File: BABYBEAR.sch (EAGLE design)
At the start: 63 parts, among them IC1 ATMEGA1284P, IC2 ATMEGA16U2-MU, IC3 MC33269DT-5.0, IC4 LM358D, IC5 LP2985-33DBVR, J1 Power, J2 Analog, J3 Digital_8_13, J4 Digital_0_7, J5 DC_2_1MM, P1 USB-6PSMT, P2 ICSP:MAIN, P3 ICSP:USB, P5V M01SMD, Q1 FDN340P, Q2 2N7002, X1 16MHz, X2 16MHz

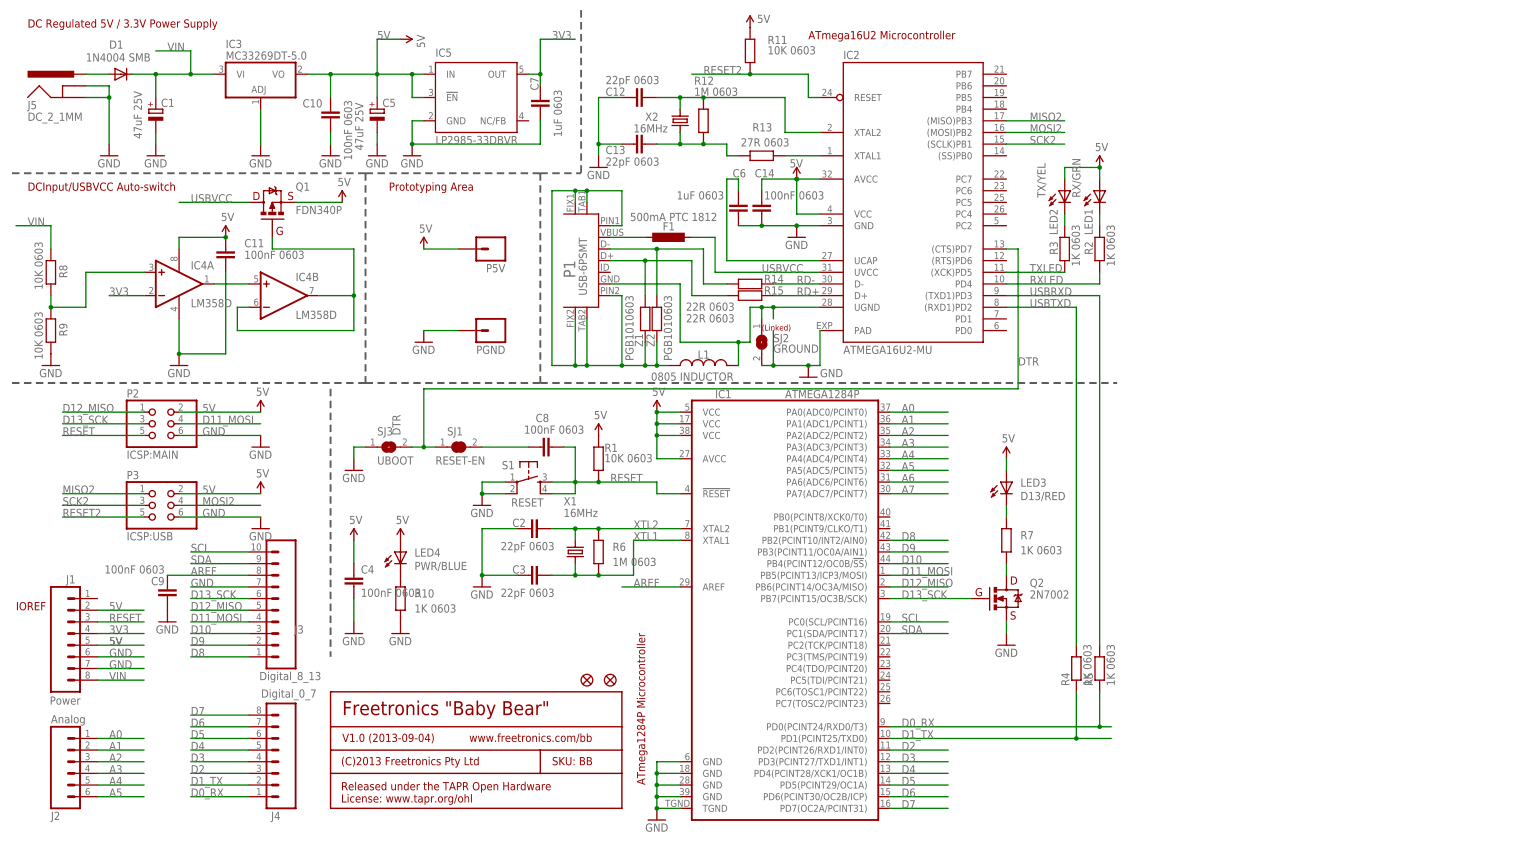
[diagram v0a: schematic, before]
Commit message: Changed USB connector to USB-C for v2.0 release
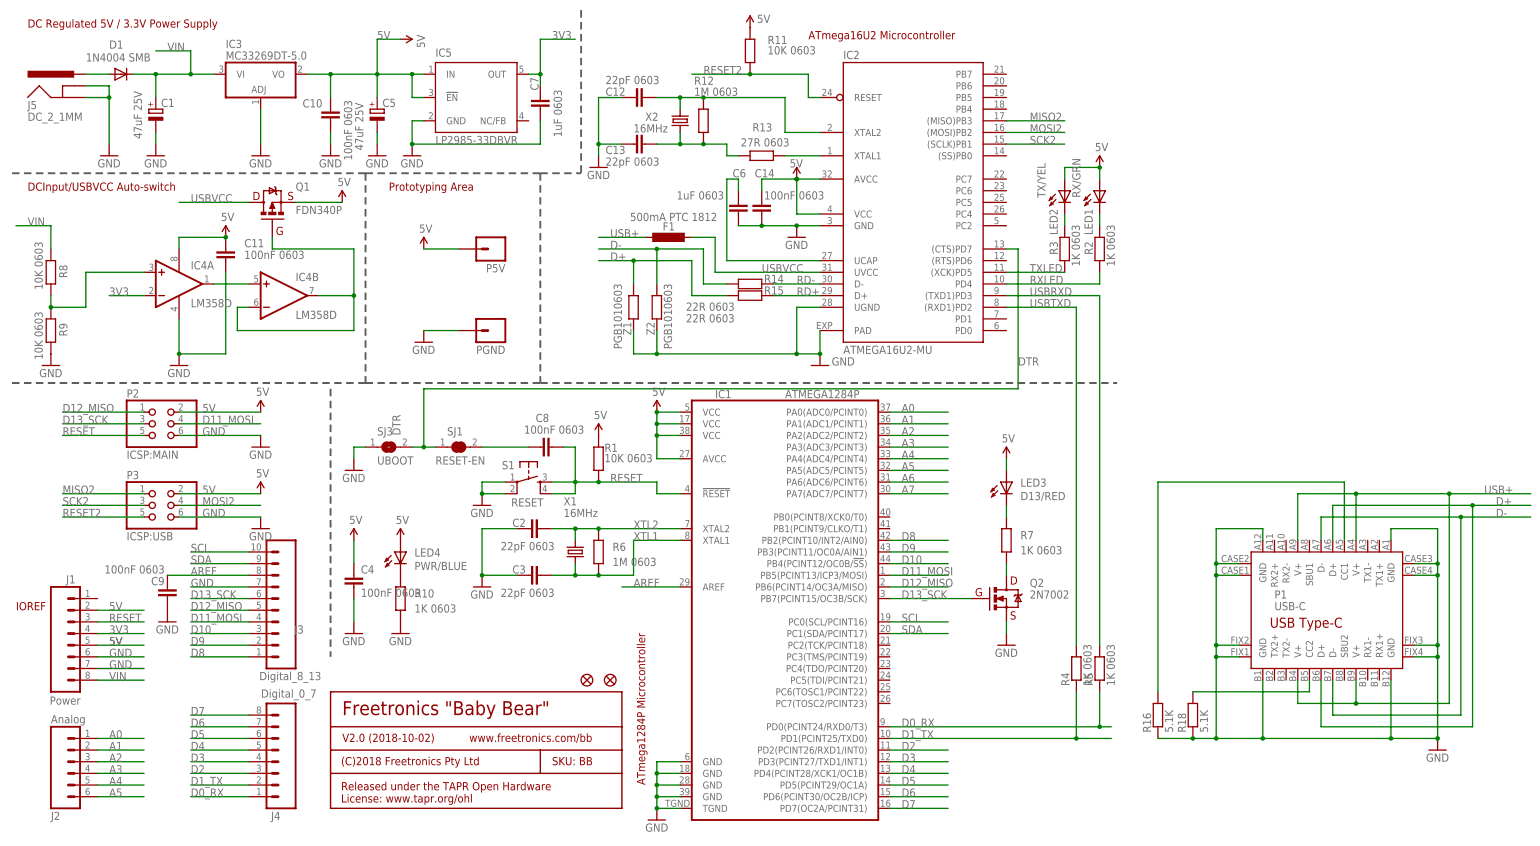
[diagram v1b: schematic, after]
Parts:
- removed L1: 0805 INDUCTOR, freetronics-master-v1:INDUCTOR0805-LARGE
- removed SJ2: GROUND, jumper:SJ
- added R16, R18: 5.1K, freetronics-original:RESISTOR0603
- J5: device freetronics:POWER_JACKPTH -> freetronics-jon:POWER_JACKPTH_SLOTS
- P1: value USB-6PSMT -> USB-C; device freetronics-jon:USB-6PSMT -> freetronics-jon:USB-C
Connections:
- removed net N$115: F1.1, P1.VBUS
- removed net N$16: P1.D+, R15.2, Z1.1
- removed net N$17: P1.D-, R14.2, Z2.1
- removed net UGND: IC2.UGND, L1.2, P1.GND, SJ2.1
- new net D+: P1.D+@A6, P1.D+@B6, R15.2, Z1.1
- new net D-: P1.D-@A7, P1.D-@B7, R14.2, Z2.1
- new net N$7: P1.CC1, R16.2
- new net USB+: F1.1, P1.V+@A4, P1.V+@A9, P1.V+@B4, P1.V+@B9
- net GND: now also IC2.UGND, P1.GND@A1, P1.GND@A12, P1.GND@B1, P1.GND@B12, P1.GND@CASE1, P1.GND@CASE2, P1.GND@CASE3, P1.GND@CASE4, P1.GND@FIX1, P1.GND@FIX2, P1.GND@FIX3, P1.GND@FIX4, R16.1, R18.1, Z1.2, Z2.2; no longer SJ2.2
- net N$3: now also P1.CC2, R18.2; no longer L1.1, P1.FIX1, P1.FIX2, P1.PIN1, P1.PIN2, P1.TAB1, P1.TAB2, Z1.2, Z2.2
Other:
- note added: "(C)2018 Freetronics Pty Ltd"
- note added: "V2.0 (2018-10-02)"
- note removed: "(C)2013 Freetronics Pty Ltd"
- note removed: "(Linked)"
- note removed: "V1.0 (2013-09-04)"
- moved on the sheet: Z1, Z2
